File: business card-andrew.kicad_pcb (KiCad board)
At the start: 2 copper layers, 85.2 x 54.2 mm, 5 parts, among them U1 NT3H2211W0FTT

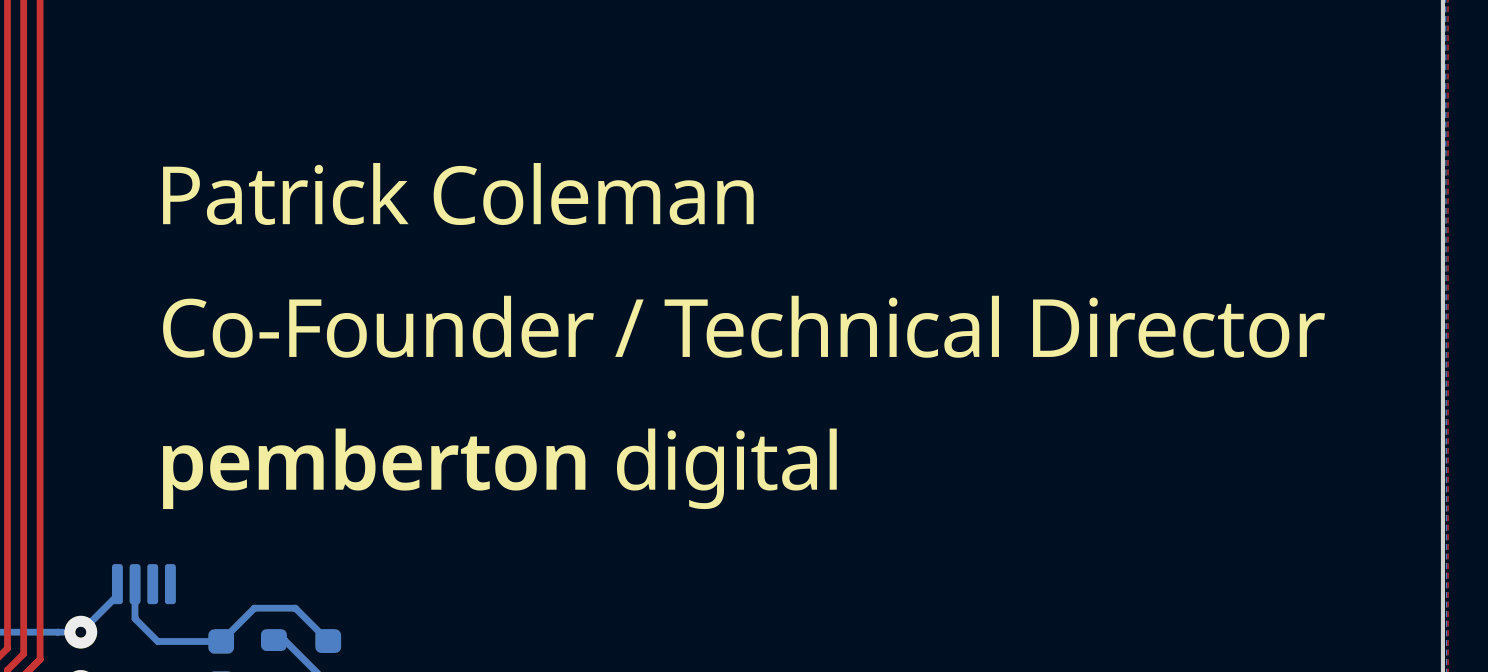
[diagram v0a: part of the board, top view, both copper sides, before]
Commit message: add business card working files
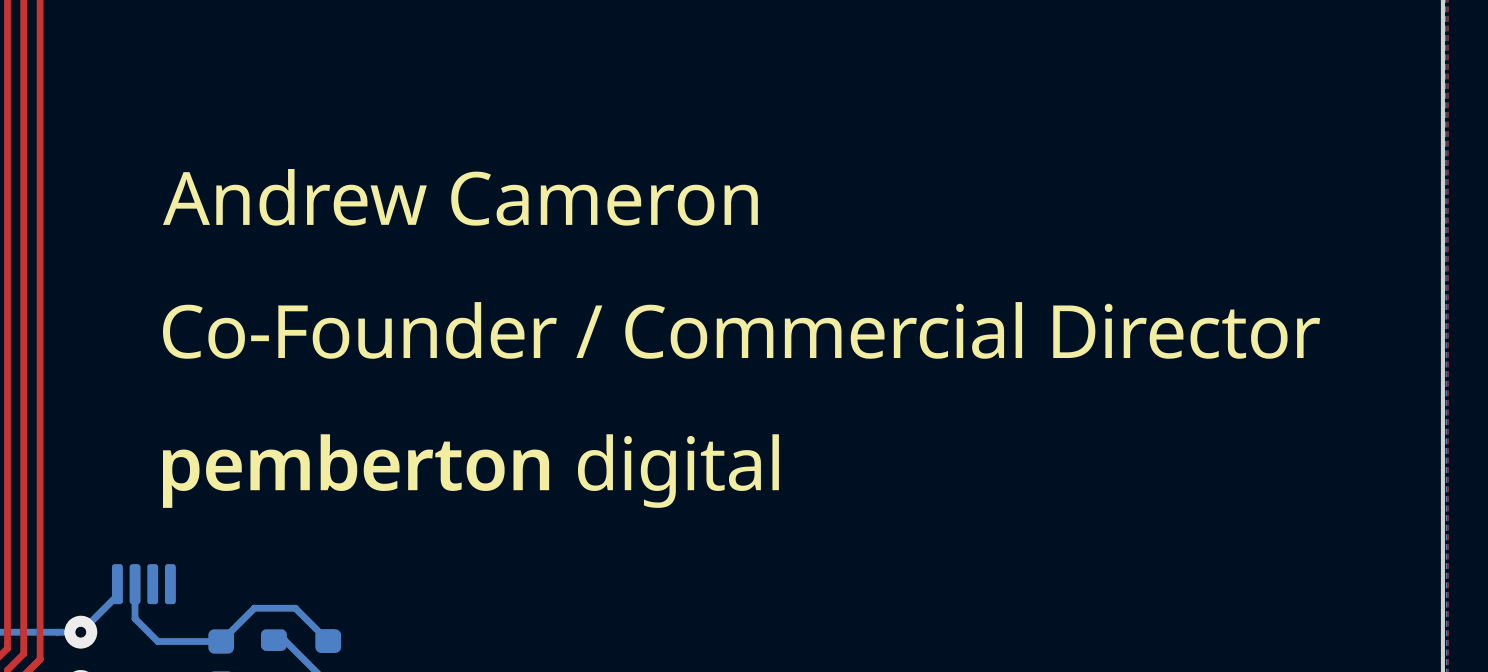
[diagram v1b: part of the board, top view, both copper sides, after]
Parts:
- U1: value NT3H2211W0FTT -> NT3H1101_NT3H1201
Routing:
- net Net-(L1-Pad2): track 0.00 -> 711.0 mm, vias 0 -> 3
- net Net-(L1-Pad1): track 711.0 -> 0.00 mm, vias 3 -> 0
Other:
- board text removed: "--- This is a V-Scoring line"
- board text removed: "<-- This is a V-Scoring line"
- board text removed: "<-- This side routed"
- board text removed: "This is a V-Scoring line ---"
- board text removed: "This side routed -->"
